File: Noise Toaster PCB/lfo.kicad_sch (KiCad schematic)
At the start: 16 parts, among them U2 LM324

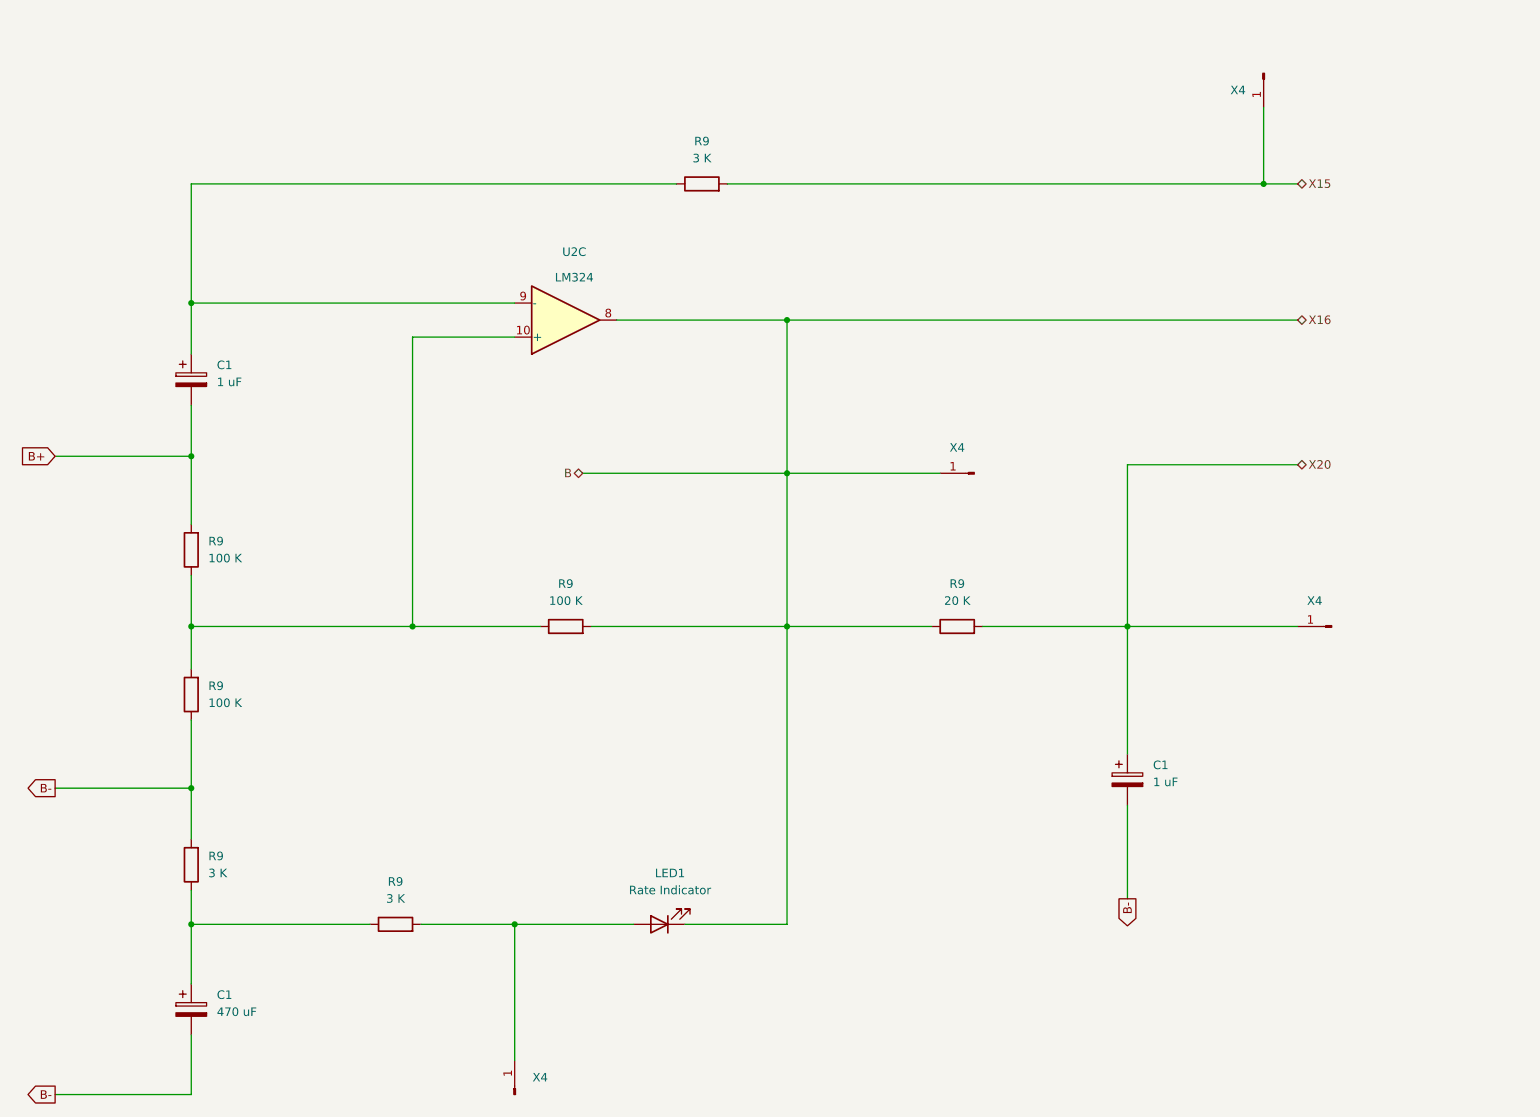
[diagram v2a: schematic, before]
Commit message: refactored schematics and added front panel
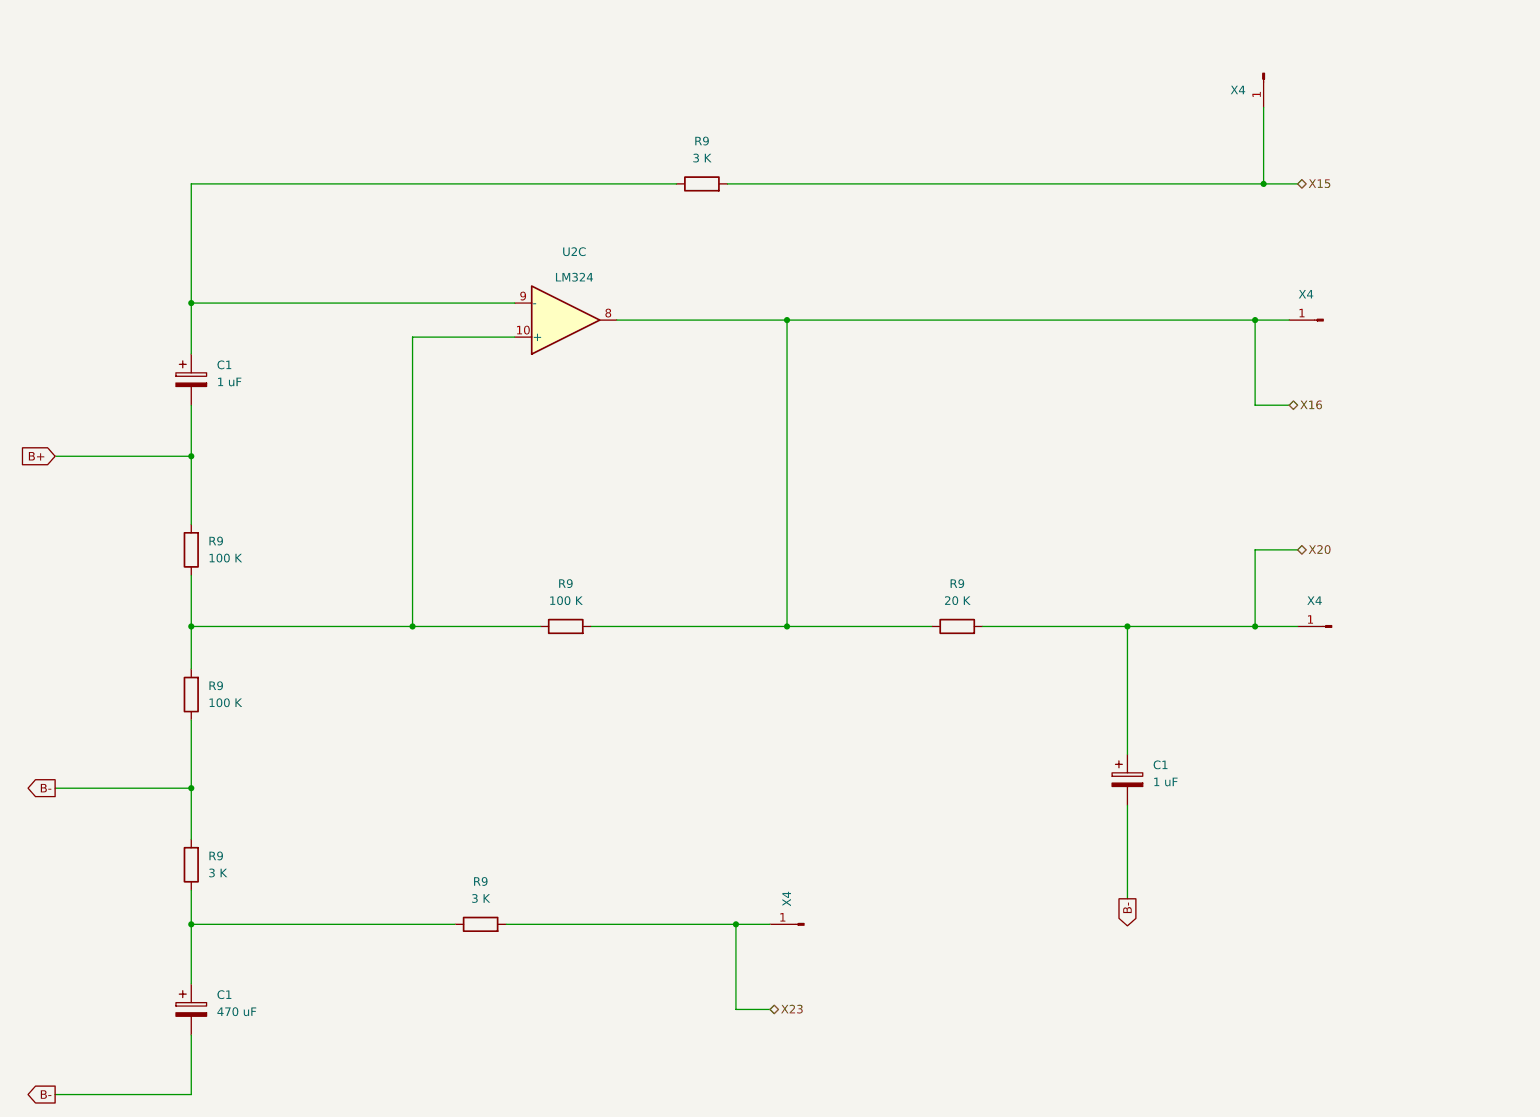
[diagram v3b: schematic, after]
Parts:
- removed LED1: Rate Indicator, symbol Device:LED
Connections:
- net X23: now reaches R9.2, X4.1 (Pin_1)
- net B renamed X16
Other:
- moved on the sheet: R9, X4
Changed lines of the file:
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@@
     (comment 3 "Music From Outer Space LLC")
   )
+  (junction (at 152.4 62.23) (diameter 0) (color 0 0 0 0)
+  )
+  (junction (at 144.78 152.4) (diameter 0) (color 0 0 0 0)
+  )
   (junction (at 203.2 107.95) (diameter 0) (color 0 0 0 0)
   )
-  (junction (at 152.4 85.09) (diameter 0) (color 0 0 0 0)
+  (junction (at 222.25 62.23) (diameter 0) (color 0 0 0 0)
   )
   (junction (at 63.5 59.69) (diameter 0) (color 0 0 0 0)
@@
   (junction (at 96.52 107.95) (diameter 0) (color 0 0 0 0)
   )
-  (junction (at 152.4 62.23) (diameter 0) (color 0 0 0 0)
-  )
-  (junction (at 111.76 152.4) (diameter 0) (color 0 0 0 0)
-  )
   (junction (at 223.52 41.91) (diameter 0) (color 0 0 0 0)
   )
@@
   (junction (at 152.4 107.95) (diameter 0) (color 0 0 0 0)
   )
+  (junction (at 222.25 107.95) (diameter 0) (color 0 0 0 0)
+  )
   (wire (pts (xy 143.51 41.91) (xy 223.52 41.91))
     (stroke (width 0) (type default))
@@
     (stroke (width 0) (type default))
   )
-  (wire (pts (xy 111.76 152.4) (xy 129.54 152.4))
+  (wire (pts (xy 222.25 74.93) (xy 222.25 62.23))
     (stroke (width 0) (type default))
   )
@@
     (stroke (width 0) (type default))
   )
+  (wire (pts (xy 203.2 107.95) (xy 222.25 107.95))
+    (stroke (width 0) (type default))
+  )
   (wire (pts (xy 63.5 168.91) (xy 63.5 177.8))
     (stroke (width 0) (type default))
   )
+  (wire (pts (xy 222.25 62.23) (xy 227.33 62.23))
+    (stroke (width 0) (type default))
+  )
   (wire (pts (xy 63.5 132.08) (xy 63.5 139.7))
     (stroke (width 0) (type default))
   )
-  (wire (pts (xy 228.6 83.82) (xy 203.2 83.82))
-    (stroke (width 0) (type default))
-  )
-  (wire (pts (xy 111.76 152.4) (xy 111.76 172.72))
+  (wire (pts (xy 149.86 165.1) (xy 144.78 165.1))
     (stroke (width 0) (type default))
   )
@@
     (stroke (width 0) (type default))
   )
-  (wire (pts (xy 175.26 85.09) (xy 152.4 85.09))
+  (wire (pts (xy 227.33 74.93) (xy 222.25 74.93))
+    (stroke (width 0) (type default))
+  )
+  (wire (pts (xy 152.4 62.23) (xy 222.25 62.23))
     (stroke (width 0) (type default))
   )
@@
     (stroke (width 0) (type default))
   )
-  (wire (pts (xy 152.4 62.23) (xy 228.6 62.23))
+  (wire (pts (xy 144.78 152.4) (xy 149.86 152.4))
     (stroke (width 0) (type default))
   )
@@
     (stroke (width 0) (type default))
   )
-  (wire (pts (xy 97.79 152.4) (xy 111.76 152.4))
+  (wire (pts (xy 110.49 152.4) (xy 144.78 152.4))
+    (stroke (width 0) (type default))
+  )
+  (wire (pts (xy 144.78 165.1) (xy 144.78 152.4))
     (stroke (width 0) (type default))
   )
@@
     (stroke (width 0) (type default))
   )
-  (wire (pts (xy 152.4 62.23) (xy 152.4 85.09))
+  (wire (pts (xy 152.4 62.23) (xy 152.4 107.95))
     (stroke (width 0) (type default))
   )
@@
     (stroke (width 0) (type default))
   )
-  (wire (pts (xy 152.4 152.4) (xy 137.16 152.4))
+  (wire (pts (xy 222.25 107.95) (xy 228.6 107.95))
     (stroke (width 0) (type default))
   )
@@
     (stroke (width 0) (type default))
   )
-  (wire (pts (xy 152.4 107.95) (xy 152.4 152.4))
-    (stroke (width 0) (type default))
-  )
   (wire (pts (xy 228.6 41.91) (xy 223.52 41.91))
     (stroke (width 0) (type default))
@@
     (stroke (width 0) (type default))
   )
-  (wire (pts (xy 63.5 152.4) (xy 90.17 152.4))
+  (wire (pts (xy 63.5 152.4) (xy 102.87 152.4))
     (stroke (width 0) (type default))
   )
@@
     (stroke (width 0) (type default))
   )
-  (wire (pts (xy 203.2 83.82) (xy 203.2 107.95))
-    (stroke (width 0) (type default))
-  )
-  (wire (pts (xy 121.92 85.09) (xy 152.4 85.09))
+  (wire (pts (xy 222.25 96.52) (xy 222.25 107.95))
+    (stroke (width 0) (type default))
+  )
+  (wire (pts (xy 222.25 96.52) (xy 228.6 96.52))
     (stroke (width 0) (type default))
   )
@@
     (stroke (width 0) (type default))
   )
-  (wire (pts (xy 203.2 107.95) (xy 228.6 107.95))
-    (stroke (width 0) (type default))
-  )
   (wire (pts (xy 127 62.23) (xy 152.4 62.23))
     (stroke (width 0) (type default))
@@
   )
   (wire (pts (xy 223.52 30.48) (xy 223.52 41.91))
-    (stroke (width 0) (type default))
-  )
-  (wire (pts (xy 152.4 85.09) (xy 152.4 107.95))
     (stroke (width 0) (type default))
   )
@@
     (effects (font (size 1.27 1.27)) (justify left))
   )
-  (hierarchical_label "X16" (shape bidirectional) (at 228.6 62.23 0) (fields_autoplaced)
+  (hierarchical_label "X23" (shape bidirectional) (at 149.86 165.1 0) (fields_autoplaced)
     (effects (font (size 1.27 1.27)) (justify left))
   )
-  (hierarchical_label "X20" (shape bidirectional) (at 228.6 83.82 0) (fields_autoplaced)
+  (hierarchical_label "X16" (shape bidirectional) (at 227.33 74.93 0) (fields_autoplaced)
     (effects (font (size 1.27 1.27)) (justify left))
   )
-  (hierarchical_label "B" (shape bidirectional) (at 121.92 85.09 180) (fields_autoplaced)
-    (effects (font (size 1.27 1.27)) (justify right))
-  )
-  (symbol (lib_id "Device:R") (at 93.98 152.4 90) (unit 1)
-    (in_bom yes) (on_board yes) (dnp no) (fields_autoplaced)
-    (property "Reference" "R9" (at 93.98 146.05 90)
-      (effects (font (size 1.27 1.27)))
-    )
-    (property "Value" "3 K" (at 93.98 148.59 90)
-      (effects (font (size 1.27 1.27)))
-    )
-    (property "Footprint" "" (at 93.98 154.178 90)
-      (effects (font (size 1.27 1.27)) hide)
-    )
-    (property "Datasheet" "~" (at 93.98 152.4 0)
+  (hierarchical_label "X20" (shape bidirectional) (at 228.6 96.52 0) (fields_autoplaced)
+    (effects (font (size 1.27 1.27)) (justify left))
+  )
+  (symbol (lib_id "Device:R") (at 106.68 152.4 90) (unit 1)
+    (in_bom yes) (on_board yes) (dnp no) (fields_autoplaced)
+    (property "Reference" "R9" (at 106.68 146.05 90)
+      (effects (font (size 1.27 1.27)))
+    )
+    (property "Value" "3 K" (at 106.68 148.59 90)
+      (effects (font (size 1.27 1.27)))
+    )
+    (property "Footprint" "" (at 106.68 154.178 90)
+      (effects (font (size 1.27 1.27)) hide)
+    )
+    (property "Datasheet" "~" (at 106.68 152.4 0)
       (effects (font (size 1.27 1.27)) hide)
     )
@@
     )
   )
-  (symbol (lib_id "Connector:Conn_01x01_Pin") (at 180.34 85.09 180) (unit 1)
+  (symbol (lib_id "Connector:Conn_01x01_Pin") (at 232.41 62.23 180) (unit 1)
     (in_bom yes) (on_board yes) (dnp no)
-    (property "Reference" "X4" (at 177.8 81.28 0)
-      (effects (font (size 1.27 1.27)))
-    )
-    (property "Value" "~" (at 179.705 87.63 0)
-      (effects (font (size 1.27 1.27)))
-    )
-    (property "Footprint" "" (at 180.34 85.09 0)
-      (effects (font (size 1.27 1.27)) hide)
-    )
-    (property "Datasheet" "~" (at 180.34 85.09 0)
+    (property "Reference" "X4" (at 229.87 58.42 0)
+      (effects (font (size 1.27 1.27)))
+    )
+    (property "Value" "~" (at 231.775 64.77 0)
+      (effects (font (size 1.27 1.27)))
+    )
+    (property "Footprint" "" (at 232.41 62.23 0)
+      (effects (font (size 1.27 1.27)) hide)
+    )
+    (property "Datasheet" "~" (at 232.41 62.23 0)
       (effects (font (size 1.27 1.27)) hide)
     )
@@
     )
   )
-  (symbol (lib_id "Connector:Conn_01x01_Pin") (at 111.76 177.8 90) (unit 1)
+  (symbol (lib_id "Connector:Conn_01x01_Pin") (at 154.94 152.4 180) (unit 1)
     (in_bom yes) (on_board yes) (dnp no)
-    (property "Reference" "X4" (at 115.57 175.26 90)
-      (effects (font (size 1.27 1.27)))
-    )
-    (property "Value" "~" (at 109.22 177.165 0)
-      (effects (font (size 1.27 1.27)))
-    )
-    (property "Footprint" "" (at 111.76 177.8 0)
-      (effects (font (size 1.27 1.27)) hide)
-    )
-    (property "Datasheet" "~" (at 111.76 177.8 0)
+    (property "Reference" "X4" (at 152.4 148.59 90)
+      (effects (font (size 1.27 1.27)))
+    )
+    (property "Value" "~" (at 154.305 154.94 0)
+      (effects (font (size 1.27 1.27)))
+    )
+    (property "Footprint" "" (at 154.94 152.4 0)
+      (effects (font (size 1.27 1.27)) hide)
+    )
+    (property "Datasheet" "~" (at 154.94 152.4 0)
       (effects (font (size 1.27 1.27)) hide)
     )
@@
         )
       )
-    )
-  )
-  (symbol (lib_id "Device:LED") (at 133.35 152.4 180) (unit 1)
-    (in_bom yes) (on_board yes) (dnp no) (fields_autoplaced)
-    (property "Reference" "LED1" (at 134.9375 144.78 0)
-      (effects (font (size 1.27 1.27)))
-    )
-    (property "Value" "Rate Indicator" (at 134.9375 147.32 0)
-      (effects (font (size 1.27 1.27)))
-    )
-    (property "Footprint" "" (at 133.35 152.4 0)
-      (effects (font (size 1.27 1.27)) hide)
-    )
-    (property "Datasheet" "~" (at 133.35 152.4 0)
-      (effects (font (size 1.27 1.27)) hide)
-    )
-    (pin "1")
-    (pin "2")
-    (instances
-      (project "Noise Toaster PCB"
-        (path "/7be3f398-d902-4566-9ee4-0bff072cd47e/465a87be-a0e4-4719-a2f2-a0657e4419e8"
-          (reference "LED1") (unit 1)
-        )
-      )
